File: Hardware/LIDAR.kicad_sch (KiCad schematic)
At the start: 0 parts

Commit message: Checkpoint
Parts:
- added J18: LIDAR, Connector_PinHeader_2.54mm:PinHeader_1x08_P2.54mm_Horizontal, symbol Connector_Generic:Conn_01x08
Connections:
- net RX: now also J18.6 (Pin_6)
- net SCL: now also J18.1 (Pin_1)
- net SDA: now also J18.2 (Pin_2)
- net TX/DATA_READY: now also J18.5 (Pin_5)
- net VDD: now also J18.4 (Pin_4), J18.8 (Pin_8)
- new net GND: J18.3 (Pin_3), J18.7 (Pin_7)
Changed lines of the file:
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@@
 (kicad_sch (version 20230121) (generator eeschema)
   (paper "A4")
-  (hierarchical_label "SDA" (shape bidirectional) (at 127 83.82 0) (fields_autoplaced)
-    (effects (font (size 1.27 1.27)) (justify left))
+  (hierarchical_label "SDA" (shape bidirectional) (at 142.24 91.44 180) (fields_autoplaced)
+    (effects (font (size 1.27 1.27)) (justify right))
   )
-  (hierarchical_label "SCL" (shape bidirectional) (at 127 86.36 0) (fields_autoplaced)
-    (effects (font (size 1.27 1.27)) (justify left))
+  (hierarchical_label "SCL" (shape bidirectional) (at 142.24 88.9 180) (fields_autoplaced)
+    (effects (font (size 1.27 1.27)) (justify right))
   )
-  (hierarchical_label "TX{slash}DATA_READY" (shape output) (at 127 81.28 0) (fields_autoplaced)
-    (effects (font (size 1.27 1.27)) (justify left))
+  (hierarchical_label "TX{slash}DATA_READY" (shape output) (at 142.24 99.06 180) (fields_autoplaced)
+    (effects (font (size 1.27 1.27)) (justify right))
   )
-  (hierarchical_label "VCC_LED" (shape passive) (at 127 73.66 0) (fields_autoplaced)
-    (effects (font (size 1.27 1.27)) (justify left))
+  (hierarchical_label "RX" (shape input) (at 142.24 101.6 180) (fields_autoplaced)
+    (effects (font (size 1.27 1.27)) (justify right))
   )
-  (hierarchical_label "RX" (shape input) (at 127 78.74 0) (fields_autoplaced)
-    (effects (font (size 1.27 1.27)) (justify left))
+  (hierarchical_label "VDD" (shape passive) (at 142.24 96.52 180) (fields_autoplaced)
+    (effects (font (size 1.27 1.27)) (justify right))
   )
-  (hierarchical_label "VDD" (shape passive) (at 127 76.2 0) (fields_autoplaced)
-    (effects (font (size 1.27 1.27)) (justify left))
+  (hierarchical_label "VDD" (shape passive) (at 142.24 106.68 180) (fields_autoplaced)
+    (effects (font (size 1.27 1.27)) (justify right))
+  )
+  (symbol (lib_id "Connector_Generic:Conn_01x08") (at 147.32 96.52 0) (unit 1)
+    (in_bom yes) (on_board yes) (dnp no) (fields_autoplaced)
+    (property "Reference" "J18" (at 149.86 96.52 0)
+      (effects (font (size 1.27 1.27)) (justify left))
+    )
+    (property "Value" "LIDAR" (at 149.86 99.06 0)
+      (effects (font (size 1.27 1.27)) (justify left))
+    )
+    (property "Footprint" "Connector_PinHeader_2.54mm:PinHeader_1x08_P2.54mm_Horizontal" (at 147.32 96.52 0)
+      (effects (font (size 1.27 1.27)) hide)
+    )
+    (property "Datasheet" "~" (at 147.32 96.52 0)
+      (effects (font (size 1.27 1.27)) hide)
+    )
+    (pin "1")
+    (pin "2")
+    (pin "3")
+    (pin "4")
+    (pin "5")
+    (pin "6")
+    (pin "7")
+    (pin "8")
+    (instances
+      (project "Avionus_Flight_Controller"
+        (path "/ddc7e940-0588-4587-8902-8ced9e615ace/885989c2-2ebd-4bec-a075-370ce9d8b265"
+          (reference "J18") (unit 1)
+        )
+      )
+    )
+  )
+  (symbol (lib_id "power:GND") (at 142.24 104.14 270) (unit 1)
+    (in_bom yes) (on_board yes) (dnp no) (fields_autoplaced)
+    (property "Reference" "#PWR052" (at 135.89 104.14 0)
+      (effects (font (size 1.27 1.27)) hide)
+    )
+    (property "Value" "GND" (at 138.43 104.14 90)
+      (effects (font (size 1.27 1.27)) (justify right))
+    )
+    (property "Footprint" "" (at 142.24 104.14 0)
+      (effects (font (size 1.27 1.27)) hide)
+    )
+    (property "Datasheet" "" (at 142.24 104.14 0)
+      (effects (font (size 1.27 1.27)) hide)
+    )
+    (pin "1")
+    (instances
+      (project "Avionus_Flight_Controller"
+        (path "/ddc7e940-0588-4587-8902-8ced9e615ace/885989c2-2ebd-4bec-a075-370ce9d8b265"
+          (reference "#PWR052") (unit 1)
+        )
+      )
+    )
+  )
+  (symbol (lib_id "power:GND") (at 142.24 93.98 270) (unit 1)
+    (in_bom yes) (on_board yes) (dnp no) (fields_autoplaced)
+    (property "Reference" "#PWR053" (at 135.89 93.98 0)
+      (effects (font (size 1.27 1.27)) hide)
+    )
+    (property "Value" "GND" (at 138.43 93.98 90)
+      (effects (font (size 1.27 1.27)) (justify right))
+    )
+    (property "Footprint" "" (at 142.24 93.98 0)
+      (effects (font (size 1.27 1.27)) hide)
+    )
+    (property "Datasheet" "" (at 142.24 93.98 0)
+      (effects (font (size 1.27 1.27)) hide)
+    )
+    (pin "1")
+    (instances
+      (project "Avionus_Flight_Controller"
+        (path "/ddc7e940-0588-4587-8902-8ced9e615ace/885989c2-2ebd-4bec-a075-370ce9d8b265"
+          (reference "#PWR053") (unit 1)
+        )
+      )
+    )
   )
 )

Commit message: Checkpoint
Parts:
- renumbered J18 to J1401
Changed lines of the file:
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@@
   (symbol (lib_id "Connector_Generic:Conn_01x08") (at 147.32 96.52 0) (unit 1)
     (in_bom yes) (on_board yes) (dnp no) (fields_autoplaced)
-    (property "Reference" "J18" (at 149.86 96.52 0)
+    (property "Reference" "J1401" (at 149.86 96.52 0)
       (effects (font (size 1.27 1.27)) (justify left))
     )
@@
       (project "Avionus_Flight_Controller"
         (path "/ddc7e940-0588-4587-8902-8ced9e615ace/885989c2-2ebd-4bec-a075-370ce9d8b265"
-          (reference "J18") (unit 1)
+          (reference "J1401") (unit 1)
         )
       )
@@
   (symbol (lib_id "power:GND") (at 142.24 104.14 270) (unit 1)
     (in_bom yes) (on_board yes) (dnp no) (fields_autoplaced)
-    (property "Reference" "#PWR052" (at 135.89 104.14 0)
+    (property "Reference" "#PWR01402" (at 135.89 104.14 0)
       (effects (font (size 1.27 1.27)) hide)
     )
@@
       (project "Avionus_Flight_Controller"
         (path "/ddc7e940-0588-4587-8902-8ced9e615ace/885989c2-2ebd-4bec-a075-370ce9d8b265"
-          (reference "#PWR052") (unit 1)
+          (reference "#PWR01402") (unit 1)
         )
       )
@@
   (symbol (lib_id "power:GND") (at 142.24 93.98 270) (unit 1)
     (in_bom yes) (on_board yes) (dnp no) (fields_autoplaced)
-    (property "Reference" "#PWR053" (at 135.89 93.98 0)
+    (property "Reference" "#PWR01401" (at 135.89 93.98 0)
       (effects (font (size 1.27 1.27)) hide)
     )
@@
       (project "Avionus_Flight_Controller"
         (path "/ddc7e940-0588-4587-8902-8ced9e615ace/885989c2-2ebd-4bec-a075-370ce9d8b265"
-          (reference "#PWR053") (unit 1)
+          (reference "#PWR01401") (unit 1)
         )
       )

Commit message: Checkpoint
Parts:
- added U1401: USBLC6-4SC6, Package_TO_SOT_SMD:SOT-23-6, symbol Power_Protection:USBLC6-4SC6
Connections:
- net GND: now also U1401.2 (GND)
- net RX: now also U1401.1 (I/O1)
- net SCL: now also U1401.4 (I/O3)
- net SDA: now also U1401.6 (I/O4)
- net TX/DATA_READY: now also U1401.3 (I/O2)
- net VDD: now also U1401.5 (VBUS)
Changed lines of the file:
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@@
 (kicad_sch (version 20230121) (generator eeschema)
   (paper "A4")
+  (hierarchical_label "VDD" (shape passive) (at 147.32 119.38 90) (fields_autoplaced)
+    (effects (font (size 1.27 1.27)) (justify left))
+  )
   (hierarchical_label "SDA" (shape bidirectional) (at 142.24 91.44 180) (fields_autoplaced)
+    (effects (font (size 1.27 1.27)) (justify right))
+  )
+  (hierarchical_label "TX{slash}DATA_READY" (shape output) (at 137.16 132.08 180) (fields_autoplaced)
     (effects (font (size 1.27 1.27)) (justify right))
   )
@@
   (hierarchical_label "TX{slash}DATA_READY" (shape output) (at 142.24 99.06 180) (fields_autoplaced)
     (effects (font (size 1.27 1.27)) (justify right))
+  )
+  (hierarchical_label "SCL" (shape bidirectional) (at 157.48 127 0) (fields_autoplaced)
+    (effects (font (size 1.27 1.27)) (justify left))
+  )
+  (hierarchical_label "SDA" (shape bidirectional) (at 157.48 132.08 0) (fields_autoplaced)
+    (effects (font (size 1.27 1.27)) (justify left))
   )
   (hierarchical_label "RX" (shape input) (at 142.24 101.6 180) (fields_autoplaced)
@@
   (hierarchical_label "VDD" (shape passive) (at 142.24 106.68 180) (fields_autoplaced)
     (effects (font (size 1.27 1.27)) (justify right))
+  )
+  (hierarchical_label "RX" (shape input) (at 137.16 127 180) (fields_autoplaced)
+    (effects (font (size 1.27 1.27)) (justify right))
+  )
+  (symbol (lib_id "Power_Protection:USBLC6-4SC6") (at 147.32 129.54 0) (unit 1)
+    (in_bom yes) (on_board yes) (dnp no) (fields_autoplaced)
+    (property "Reference" "U1401" (at 148.9711 116.84 0)
+      (effects (font (size 1.27 1.27)) (justify left))
+    )
+    (property "Value" "USBLC6-4SC6" (at 148.9711 119.38 0)
+      (effects (font (size 1.27 1.27)) (justify left))
+    )
+    (property "Footprint" "Package_TO_SOT_SMD:SOT-23-6" (at 147.32 142.24 0)
+      (effects (font (size 1.27 1.27)) hide)
+    )
+    (property "Datasheet" "https://www.st.com/resource/en/datasheet/usblc6-4.pdf" (at 152.4 120.65 0)
+      (effects (font (size 1.27 1.27)) hide)
+    )
+    (pin "1")
+    (pin "2")
+    (pin "3")
+    (pin "4")
+    (pin "5")
+    (pin "6")
+    (instances
+      (project "Avionus_Flight_Controller"
+        (path "/ddc7e940-0588-4587-8902-8ced9e615ace/885989c2-2ebd-4bec-a075-370ce9d8b265"
+          (reference "U1401") (unit 1)
+        )
+      )
+    )
   )
   (symbol (lib_id "Connector_Generic:Conn_01x08") (at 147.32 96.52 0) (unit 1)
@@
         )
       )
+    )
+  )
+  (symbol (lib_id "power:GND") (at 147.32 139.7 0) (unit 1)
+    (in_bom yes) (on_board yes) (dnp no) (fields_autoplaced)
+    (property "Reference" "#PWR01403" (at 147.32 146.05 0)
+      (effects (font (size 1.27 1.27)) hide)
+    )
+    (property "Value" "GND" (at 147.32 144.78 0)
+      (effects (font (size 1.27 1.27)))
+    )
+    (property "Footprint" "" (at 147.32 139.7 0)
+      (effects (font (size 1.27 1.27)) hide)
+    )
+    (property "Datasheet" "" (at 147.32 139.7 0)
+      (effects (font (size 1.27 1.27)) hide)
+    )
+    (pin "1")
+    (instances
+      (project "Avionus_Flight_Controller"
+        (path "/ddc7e940-0588-4587-8902-8ced9e615ace/885989c2-2ebd-4bec-a075-370ce9d8b265"
+          (reference "#PWR01403") (unit 1)
+        )
+      )

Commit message: Checkpoint routing
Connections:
- net SCL: now also U1401.6 (I/O4); no longer U1401.4 (I/O3)
- net SDA: now also U1401.4 (I/O3); no longer U1401.6 (I/O4)
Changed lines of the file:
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@@
     (effects (font (size 1.27 1.27)) (justify right))
   )
-  (hierarchical_label "SCL" (shape bidirectional) (at 157.48 127 0) (fields_autoplaced)
+  (hierarchical_label "SCL" (shape bidirectional) (at 157.48 132.08 0) (fields_autoplaced)
     (effects (font (size 1.27 1.27)) (justify left))
   )
-  (hierarchical_label "SDA" (shape bidirectional) (at 157.48 132.08 0) (fields_autoplaced)
+  (hierarchical_label "SDA" (shape bidirectional) (at 157.48 127 0) (fields_autoplaced)
     (effects (font (size 1.27 1.27)) (justify left))
   )

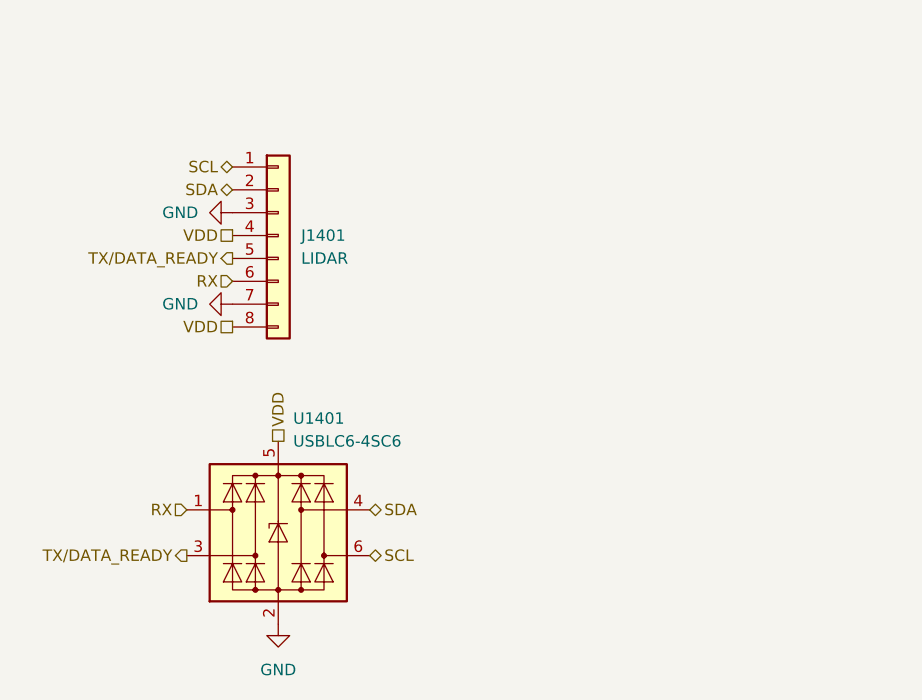
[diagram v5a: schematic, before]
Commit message: Add lidar2
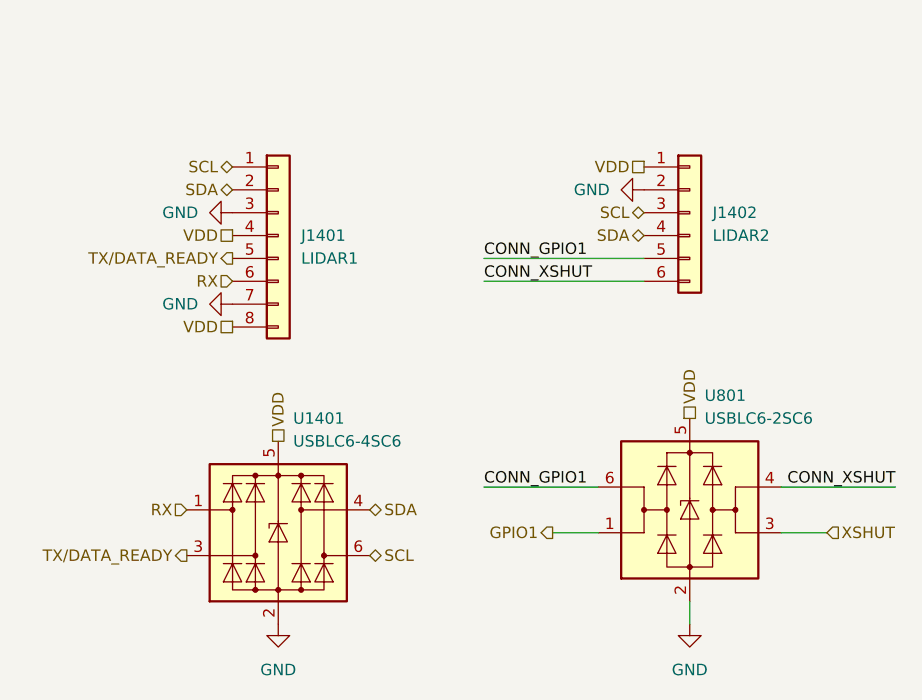
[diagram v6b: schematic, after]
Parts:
- added J1402: LIDAR2, Connector_PinHeader_2.54mm:PinHeader_1x06_P2.54mm_Horizontal, symbol Connector_Generic:Conn_01x06
- added U801: USBLC6-2SC6, Package_TO_SOT_SMD:SOT-23-6, symbol Power_Protection:USBLC6-2SC6
- J1401: value LIDAR -> LIDAR1
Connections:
- net GND: now also J1402.2 (Pin_2), U801.2 (GND)
- net SCL: now also J1402.3 (Pin_3)
- net SDA: now also J1402.4 (Pin_4)
- net VDD: now also J1402.1 (Pin_1), U801.5 (VBUS)
- new net CONN_GPIO1: J1402.5 (Pin_5), U801.6 (I/O1)
- new net CONN_XSHUT: J1402.6 (Pin_6), U801.4 (I/O2)
- new net GPIO1: U801.1 (I/O1)
- new net XSHUT: U801.3 (I/O2)
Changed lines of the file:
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@@
 (kicad_sch (version 20230121) (generator eeschema)
   (paper "A4")
+  (wire (pts (xy 208.28 129.54) (xy 203.2 129.54))
+    (stroke (width 0) (type default))
+  )
+  (wire (pts (xy 193.04 137.16) (xy 193.04 139.7))
+    (stroke (width 0) (type default))
+  )
+  (wire (pts (xy 203.2 124.46) (xy 215.9 124.46))
+    (stroke (width 0) (type default))
+  )
+  (wire (pts (xy 170.18 101.6) (xy 187.96 101.6))
+    (stroke (width 0) (type default))
+  )
+  (wire (pts (xy 182.88 124.46) (xy 170.18 124.46))
+    (stroke (width 0) (type default))
+  )
+  (wire (pts (xy 177.8 129.54) (xy 182.88 129.54))
+    (stroke (width 0) (type default))
+  )
+  (wire (pts (xy 170.18 99.06) (xy 187.96 99.06))
+    (stroke (width 0) (type default))
+  )
+  (label "CONN_XSHUT" (at 170.18 101.6 0) (fields_autoplaced)
+    (effects (font (size 1.27 1.27)) (justify left bottom))
+  )
+  (label "CONN_GPIO1" (at 170.18 124.46 0) (fields_autoplaced)
+    (effects (font (size 1.27 1.27)) (justify left bottom))
+  )
+  (label "CONN_GPIO1" (at 170.18 99.06 0) (fields_autoplaced)
+    (effects (font (size 1.27 1.27)) (justify left bottom))
+  )
+  (label "CONN_XSHUT" (at 215.9 124.46 180) (fields_autoplaced)
+    (effects (font (size 1.27 1.27)) (justify right bottom))
+  )
   (hierarchical_label "VDD" (shape passive) (at 147.32 119.38 90) (fields_autoplaced)
     (effects (font (size 1.27 1.27)) (justify left))
@@
     (effects (font (size 1.27 1.27)) (justify right))
   )
+  (hierarchical_label "SDA" (shape bidirectional) (at 187.96 96.52 180) (fields_autoplaced)
+    (effects (font (size 1.27 1.27)) (justify right))
+  )
   (hierarchical_label "SCL" (shape bidirectional) (at 142.24 88.9 180) (fields_autoplaced)
     (effects (font (size 1.27 1.27)) (justify right))
@@
     (effects (font (size 1.27 1.27)) (justify left))
   )
+  (hierarchical_label "SCL" (shape bidirectional) (at 187.96 93.98 180) (fields_autoplaced)
+    (effects (font (size 1.27 1.27)) (justify right))
+  )
+  (hierarchical_label "XSHUT" (shape input) (at 208.28 129.54 0) (fields_autoplaced)
+    (effects (font (size 1.27 1.27)) (justify left))
+  )
   (hierarchical_label "SDA" (shape bidirectional) (at 157.48 127 0) (fields_autoplaced)
     (effects (font (size 1.27 1.27)) (justify left))
   )
+  (hierarchical_label "VDD" (shape passive) (at 193.04 116.84 90) (fields_autoplaced)
+    (effects (font (size 1.27 1.27)) (justify left))
+  )
   (hierarchical_label "RX" (shape input) (at 142.24 101.6 180) (fields_autoplaced)
     (effects (font (size 1.27 1.27)) (justify right))
@@
     (effects (font (size 1.27 1.27)) (justify right))
   )
+  (hierarchical_label "VDD" (shape passive) (at 187.96 88.9 180) (fields_autoplaced)
+    (effects (font (size 1.27 1.27)) (justify right))
+  )
+  (hierarchical_label "GPIO1" (shape output) (at 177.8 129.54 180) (fields_autoplaced)
+    (effects (font (size 1.27 1.27)) (justify right))
+  )
   (hierarchical_label "VDD" (shape passive) (at 142.24 106.68 180) (fields_autoplaced)
     (effects (font (size 1.27 1.27)) (justify right))
@@
     (effects (font (size 1.27 1.27)) (justify right))
   )
-  (symbol (lib_id "Power_Protection:USBLC6-4SC6") (at 147.32 129.54 0) (unit 1)
-    (in_bom yes) (on_board yes) (dnp no) (fields_autoplaced)
-    (property "Reference" "U1401" (at 148.9711 116.84 0)
-      (effects (font (size 1.27 1.27)) (justify left))
-    )
-    (property "Value" "USBLC6-4SC6" (at 148.9711 119.38 0)
-      (effects (font (size 1.27 1.27)) (justify left))
-    )
-    (property "Footprint" "Package_TO_SOT_SMD:SOT-23-6" (at 147.32 142.24 0)
-      (effects (font (size 1.27 1.27)) hide)
-    )
-    (property "Datasheet" "https://www.st.com/resource/en/datasheet/usblc6-4.pdf" (at 152.4 120.65 0)
+  (symbol (lib_id "Connector_Generic:Conn_01x06") (at 193.04 93.98 0) (unit 1)
+    (in_bom yes) (on_board yes) (dnp no) (fields_autoplaced)
+    (property "Reference" "J1402" (at 195.58 93.98 0)
+      (effects (font (size 1.27 1.27)) (justify left))
+    )
+    (property "Value" "LIDAR2" (at 195.58 96.52 0)
+      (effects (font (size 1.27 1.27)) (justify left))
+    )
+    (property "Footprint" "Connector_PinHeader_2.54mm:PinHeader_1x06_P2.54mm_Horizontal" (at 193.04 93.98 0)
+      (effects (font (size 1.27 1.27)) hide)
+    )
+    (property "Datasheet" "~" (at 193.04 93.98 0)
       (effects (font (size 1.27 1.27)) hide)
     )
@@
       (project "Avionus_Flight_Controller"
         (path "/ddc7e940-0588-4587-8902-8ced9e615ace/885989c2-2ebd-4bec-a075-370ce9d8b265"
+          (reference "J1402") (unit 1)
+        )
+      )
+    )
+  )
+  (symbol (lib_id "Power_Protection:USBLC6-4SC6") (at 147.32 129.54 0) (unit 1)
+    (in_bom yes) (on_board yes) (dnp no) (fields_autoplaced)
+    (property "Reference" "U1401" (at 148.9711 116.84 0)
+      (effects (font (size 1.27 1.27)) (justify left))
+    )
+    (property "Value" "USBLC6-4SC6" (at 148.9711 119.38 0)
+      (effects (font (size 1.27 1.27)) (justify left))
+    )
+    (property "Footprint" "Package_TO_SOT_SMD:SOT-23-6" (at 147.32 142.24 0)
+      (effects (font (size 1.27 1.27)) hide)
+    )
+    (property "Datasheet" "https://www.st.com/resource/en/datasheet/usblc6-4.pdf" (at 152.4 120.65 0)
+      (effects (font (size 1.27 1.27)) hide)
+    )
+    (pin "1")
+    (pin "2")
+    (pin "3")
+    (pin "4")
+    (pin "5")
+    (pin "6")
+    (instances
+      (project "Avionus_Flight_Controller"
+        (path "/ddc7e940-0588-4587-8902-8ced9e615ace/885989c2-2ebd-4bec-a075-370ce9d8b265"
           (reference "U1401") (unit 1)
         )
@@
       (effects (font (size 1.27 1.27)) (justify left))
     )
-    (property "Value" "LIDAR" (at 149.86 99.06 0)
+    (property "Value" "LIDAR1" (at 149.86 99.06 0)
       (effects (font (size 1.27 1.27)) (justify left))
     )
@@
     )
   )
+  (symbol (lib_id "Power_Protection:USBLC6-2SC6") (at 193.04 127 0) (unit 1)
+    (in_bom yes) (on_board yes) (dnp no) (fields_autoplaced)
+    (property "Reference" "U801" (at 194.6911 114.3 0)
+      (effects (font (size 1.27 1.27)) (justify left))
+    )
+    (property "Value" "USBLC6-2SC6" (at 194.6911 116.84 0)
+      (effects (font (size 1.27 1.27)) (justify left))
+    )
+    (property "Footprint" "Package_TO_SOT_SMD:SOT-23-6" (at 193.04 139.7 0)
+      (effects (font (size 1.27 1.27)) hide)
+    )
+    (property "Datasheet" "https://www.st.com/resource/en/datasheet/usblc6-2.pdf" (at 198.12 118.11 0)
+      (effects (font (size 1.27 1.27)) hide)
+    )
+    (pin "1")
+    (pin "2")
+    (pin "3")
+    (pin "4")
+    (pin "5")
+    (pin "6")
+    (instances
+      (project "Avionus_Flight_Controller"
+        (path "/ddc7e940-0588-4587-8902-8ced9e615ace/d19046d9-5fb5-41f1-9a98-30f2d85e54f8"
+          (reference "U801") (unit 1)
+        )
+        (path "/ddc7e940-0588-4587-8902-8ced9e615ace/885989c2-2ebd-4bec-a075-370ce9d8b265"
+          (reference "U1402") (unit 1)
+        )
+      )
+    )
+  )
+  (symbol (lib_id "power:GND") (at 187.96 91.44 270) (unit 1)
+    (in_bom yes) (on_board yes) (dnp no) (fields_autoplaced)
+    (property "Reference" "#PWR01404" (at 181.61 91.44 0)
+      (effects (font (size 1.27 1.27)) hide)
+    )
+    (property "Value" "GND" (at 184.15 91.44 90)
+      (effects (font (size 1.27 1.27)) (justify right))
+    )
+    (property "Footprint" "" (at 187.96 91.44 0)
+      (effects (font (size 1.27 1.27)) hide)
+    )
+    (property "Datasheet" "" (at 187.96 91.44 0)
+      (effects (font (size 1.27 1.27)) hide)
+    )
+    (pin "1")
+    (instances
+      (project "Avionus_Flight_Controller"
+        (path "/ddc7e940-0588-4587-8902-8ced9e615ace/885989c2-2ebd-4bec-a075-370ce9d8b265"
+          (reference "#PWR01404") (unit 1)
+        )
+      )
+    )
+  )
   (symbol (lib_id "power:GND") (at 142.24 93.98 270) (unit 1)
     (in_bom yes) (on_board yes) (dnp no) (fields_autoplaced)
@@
         )
       )
+    )
+  )
+  (symbol (lib_name "GND_1") (lib_id "power:GND") (at 193.04 139.7 0) (unit 1)
+    (in_bom yes) (on_board yes) (dnp no) (fields_autoplaced)
+    (property "Reference" "#PWR0803" (at 193.04 146.05 0)
+      (effects (font (size 1.27 1.27)) hide)
+    )
+    (property "Value" "GND" (at 193.04 144.78 0)
+      (effects (font (size 1.27 1.27)))
+    )
+    (property "Footprint" "" (at 193.04 139.7 0)
+      (effects (font (size 1.27 1.27)) hide)
+    )
+    (property "Datasheet" "" (at 193.04 139.7 0)
+      (effects (font (size 1.27 1.27)) hide)
+    )
+    (pin "1")
+    (instances
+      (project "Avionus_Flight_Controller"
+        (path "/ddc7e940-0588-4587-8902-8ced9e615ace/d19046d9-5fb5-41f1-9a98-30f2d85e54f8"
+          (reference "#PWR0803") (unit 1)
+        )
+        (path "/ddc7e940-0588-4587-8902-8ced9e615ace/885989c2-2ebd-4bec-a075-370ce9d8b265"
+          (reference "#PWR01405") (unit 1)
+        )
+      )
